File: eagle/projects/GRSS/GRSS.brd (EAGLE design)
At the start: 66 x 50 mm, 36 parts, among them J1 MOL-SL-2-RA, J10 MOL-SL-2-RA, J11 MOL-SL-2-RA, J2 MOL-SL-2-RA, J3 MOL-SL-2-RA, J4 MOL-SL-2-RA, J5 MOL-SL-2-RA, J6 MOL-SL-2-RA, J7 MOL-SL-2-RA, J8 MOL-SL-2-RA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

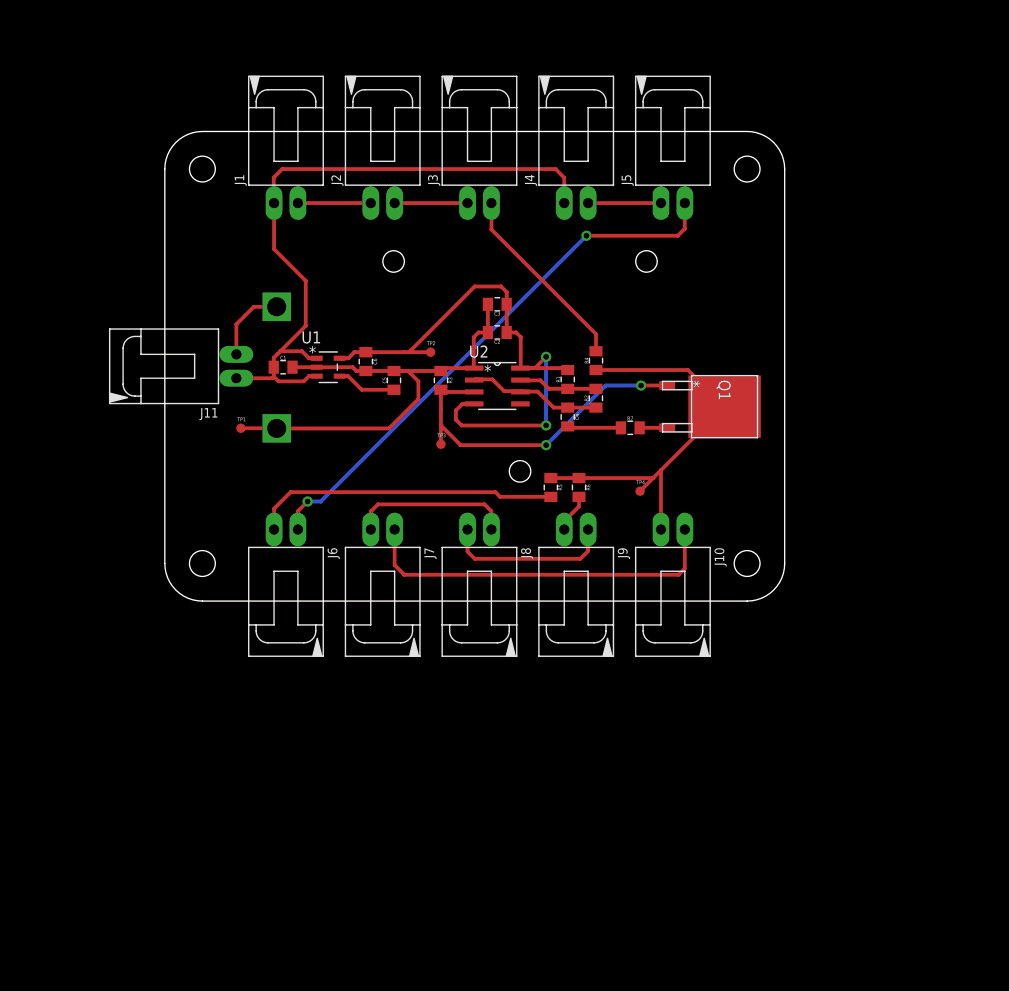
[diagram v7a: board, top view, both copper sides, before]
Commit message: Connectors now not hanging off sides, now 62x66mm2
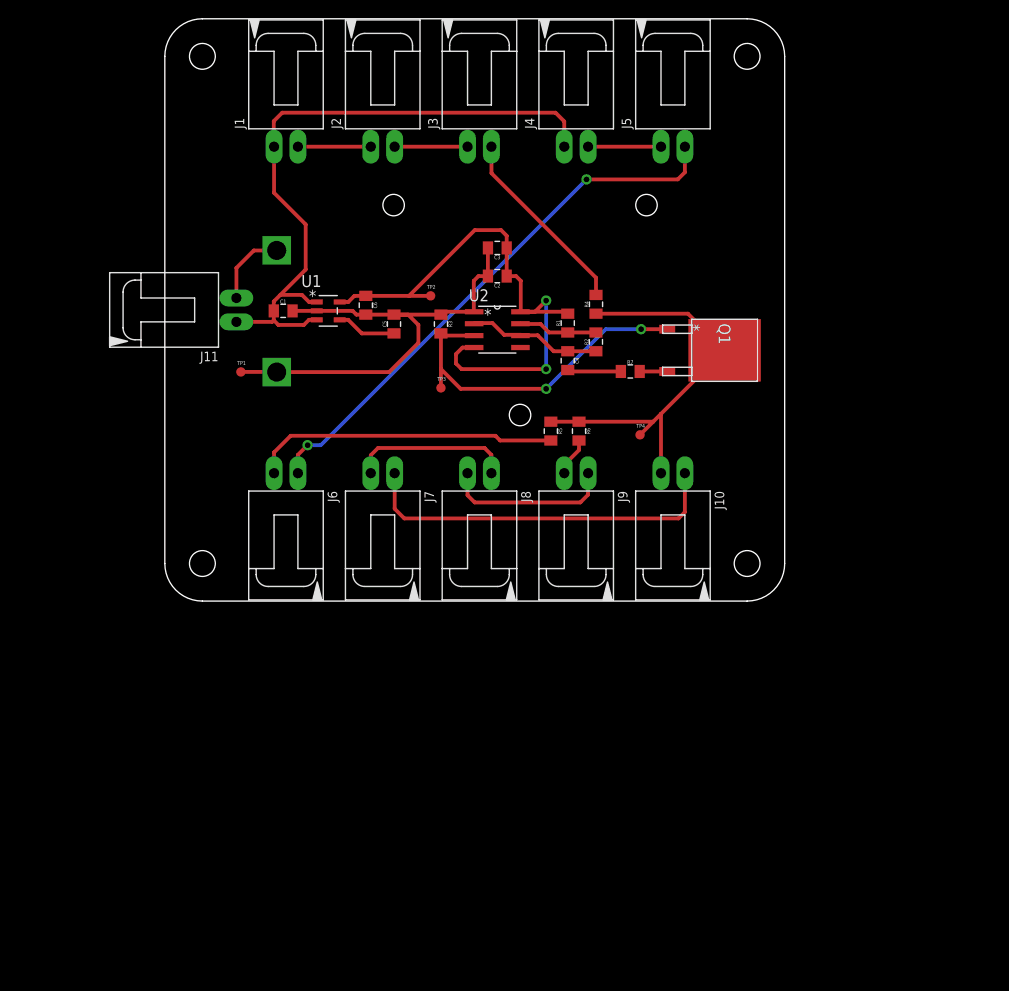
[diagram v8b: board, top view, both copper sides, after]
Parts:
- moved H3 12.0 mm to (4.00, 58.0)
- moved H4 12.0 mm to (62.0, 58.0)
- moved R5 6.00 mm to (41.1, 18.1)
- moved R6 6.00 mm to (44.1, 18.1)
- moved BATT 6.00 mm to (65.0, 16.0)
- moved C1 6.00 mm to (12.6, 30.9)
- moved C2 6.00 mm to (35.4, 34.6)
- moved C3 6.00 mm to (35.4, 37.6)
- moved C4 6.00 mm to (42.9, 25.6)
- moved C5 6.00 mm to (24.4, 29.5)
- moved C6 6.00 mm to (21.4, 31.5)
- moved J1 6.00 mm to (12.9, 56.0)
- moved J10 6.00 mm to (54.1, 6.00)
- moved J11 6.00 mm to (0.00, 31.0)
- moved J2 6.00 mm to (23.2, 56.0)
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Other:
- board size 66 x 50 mm -> 66 x 62 mm
